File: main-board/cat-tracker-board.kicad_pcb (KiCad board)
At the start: 2 copper layers, 69.5 x 29 mm, 26 parts, among them J1 Conn_01x10, J2 USB_C_Receptacle_USB2.0, J3 Conn_01x03, J4 Conn_01x02, Q5 SI3443DDV-T1-GE3, SW1 PCM12SMTR, U1 ATSAMD21E18A-A, U2 LM3480-3.3, U4 RFM95W-915S2

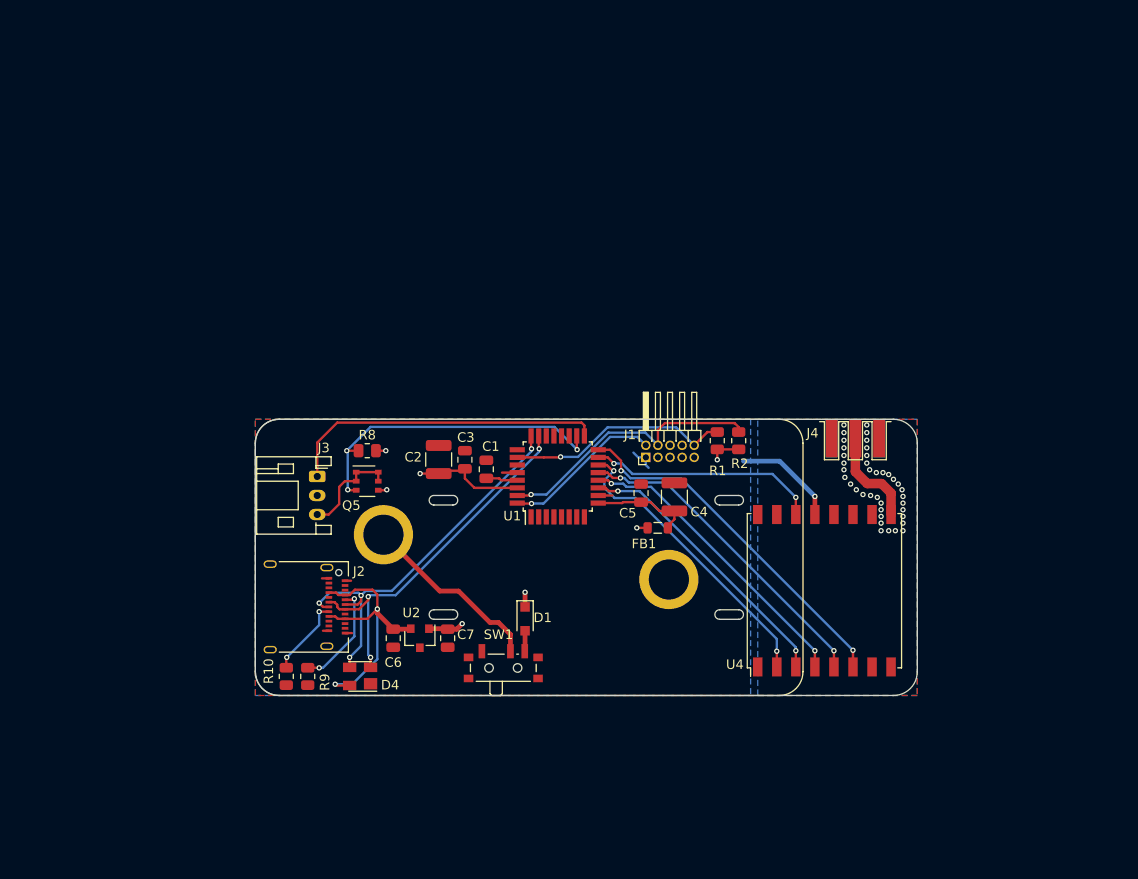
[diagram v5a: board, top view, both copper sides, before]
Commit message: Add L80 GPS, charge ic, and battery protection ic.
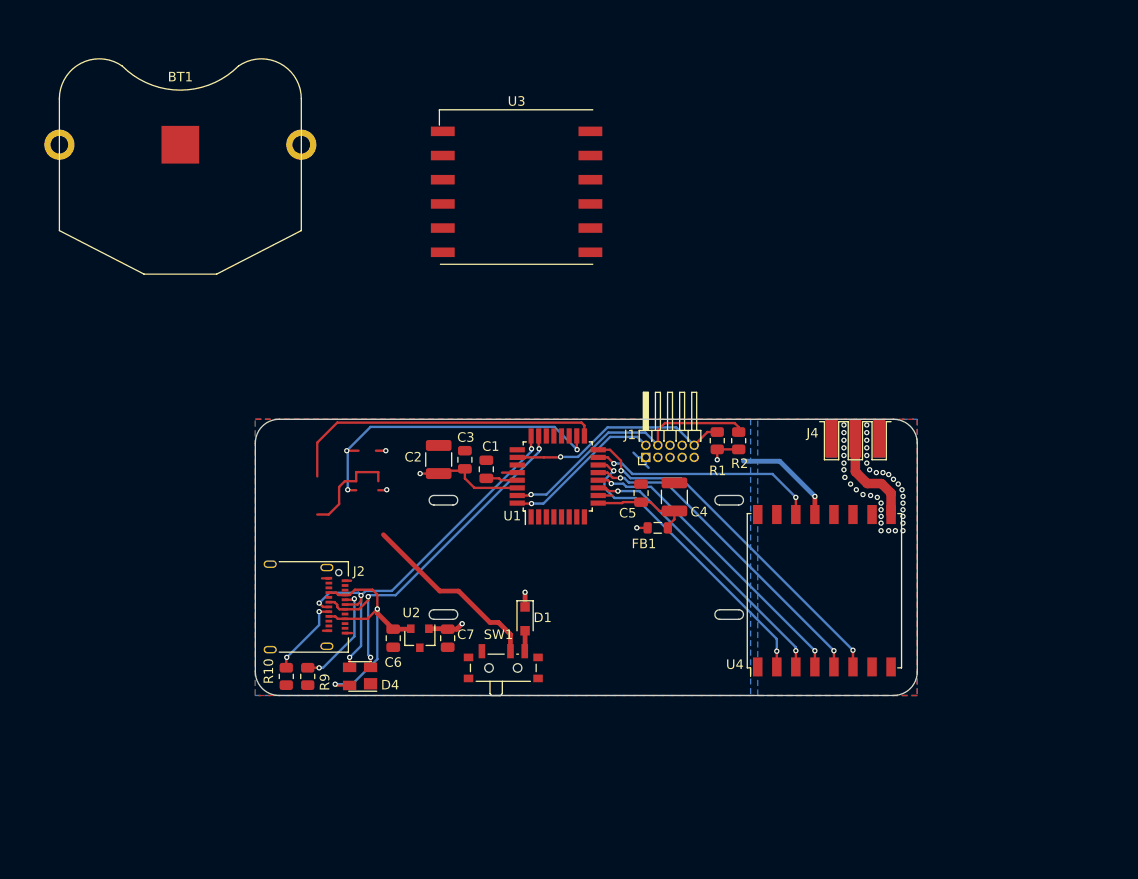
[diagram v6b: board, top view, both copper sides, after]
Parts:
- removed J3: Conn_01x03, Connector_JST:JST_PH_S3B-PH-K_1x03_P2.00mm_Horizontal
- removed Q5: SI3443DDV-T1-GE3, Package_SO:TSOP-6_1.65x3.05mm_P0.95mm
- removed R8: 100k, Resistor_SMD:R_0805_2012Metric
- added U3: L80-R, RF_GPS:Quectel_L80-R, F.Cu at (27.4, -24.4)
- BT1: value Battery -> Lir2477; footprint cat-tracker-board:battery-board -> colinholzman:Keystone_3039
- moved BT1 56.7 mm to (-7.87, -28.8)
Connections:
- U1 pad 17: /GPS_TX -> (no net)
- U1 pad 18: /GPS_EN -> (no net)
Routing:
- net (no net): track 0.00 -> 67.6 mm, vias 0 -> 3
- net /GPS_EN: track 33.9 -> 0.00 mm, vias 3 -> 0
- net /GPS_TX: track 33.7 -> 0.00 mm

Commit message: Annotate, assign footprints, and assign part numbers.
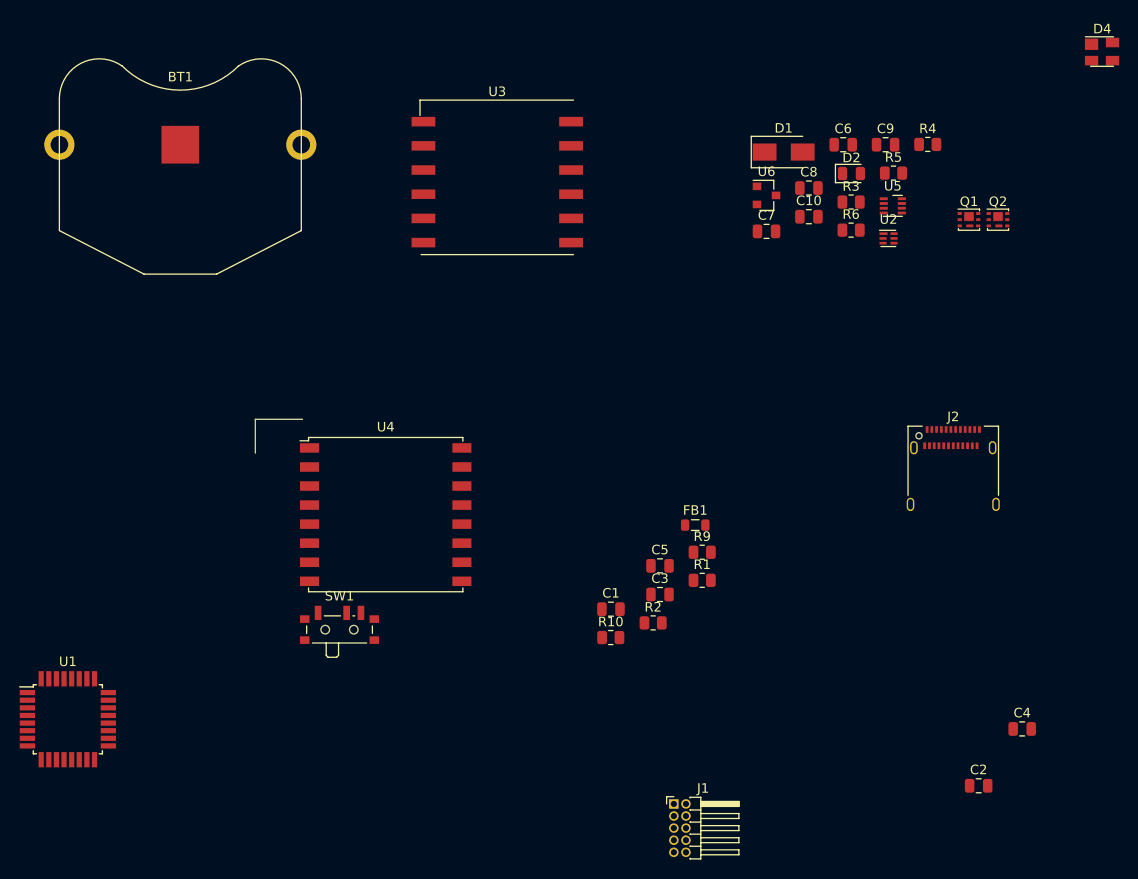
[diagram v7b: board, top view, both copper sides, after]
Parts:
- removed J4: Conn_01x02, cat-tracker-board:RF-Solutions-CON-SMA-EDGE-S
- added C10: 1 uF, Capacitor_SMD:C_0805_2012Metric, F.Cu at (58.1, -21.3)
- added C8: 0.1 uF, Capacitor_SMD:C_0805_2012Metric, F.Cu at (58.1, -24.3)
- added C9: 1 uF, Capacitor_SMD:C_0805_2012Metric, F.Cu at (66.2, -28.8)
- added D2: LED, LED_SMD:LED_0805_2012Metric, F.Cu at (62.6, -25.8)
- added Q1: CSD16301Q2, Package_SON:Texas_DQK, F.Cu at (74.9, -21.0)
- added Q2: CSD16301Q2, Package_SON:Texas_DQK, F.Cu at (78.0, -21.0)
- added R3: 2.2K, Resistor_SMD:R_0805_2012Metric, F.Cu at (62.6, -22.8)
- added R4: 330, Resistor_SMD:R_0805_2012Metric, F.Cu at (70.6, -28.9)
- added R5: 750, Resistor_SMD:R_0805_2012Metric, F.Cu at (67.0, -25.8)
- added R6: 14K, Resistor_SMD:R_0805_2012Metric, F.Cu at (62.6, -19.9)
- added U5: MCP73831-2ACI/MC, Package_DFN_QFN:DFN-8_2x2mm_P0.5mm, F.Cu at (66.9, -22.4)
- added U6: MCP1700T-3602E/TT, Package_TO_SOT_SMD:SOT-23, F.Cu at (53.7, -23.5)
- C2, C4: footprint Capacitor_SMD:C_1210_3225Metric -> Capacitor_SMD:C_0805_2012Metric
- C6, C7: value 0.1 uF -> 4.7 uF
- D1: value CUS08F30 -> SMAJ5.0A; footprint Diode_SMD:D_SOD-323_HandSoldering -> Diode_SMD:D_SMA
- J2: value USB_C_Receptacle_USB2.0 -> USB C
- U2: value LM3480-3.3 -> BQ29737DSER; footprint Package_TO_SOT_SMD:SOT-23 -> Package_SON:WSON-6_1.5x1.5mm_P0.5mm
- moved D4 101.8 mm to (88.9, -38.6), turned to 0 degrees
- moved J2 70.2 mm to (73.3, 6.10), turned to 0 degrees
- moved C6 70.1 mm to (61.7, -28.8), turned to 0 degrees
- moved C2 66.2 mm to (75.9, 38.5), turned to 0 degrees
- moved U2 64.7 mm to (66.5, -19.0), turned to 0 degrees
- moved U1 57.4 mm to (-19.7, 31.5), turned to 0 degrees
- moved D1 56.0 mm to (55.5, -28.1), turned to 0 degrees
- moved C7 54.3 mm to (53.7, -19.7), turned to 0 degrees
- moved U4 46.8 mm to (13.7, 10.0), turned to 0 degrees
- moved C4 43.9 mm to (80.5, 32.5), turned to 0 degrees
- moved R9 43.4 mm to (46.9, 14.0), turned to 0 degrees
- moved J1 36.5 mm to (43.9, 40.4), turned to 0 degrees
- moved G*** 36.4 mm to (94.0, -4.19)
- moved R10 34.3 mm to (37.3, 22.9), turned to 0 degrees
- moved C3 24.9 mm to (42.5, 18.4), turned to 0 degrees
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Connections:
- BT1 pad 2: /GND -> Net-(BT1-Pad2)
- C2 pad 1: /+3V3 -> /VDD
- C3 pad 2: /+3V3 -> /VDD
- C6 pad 1: /GND -> /VUSB
- C6 pad 2: /VUSB -> /GND
- C7 pad 1: /GND -> /VBAT
- C7 pad 2: /+3V3 -> /GND
- D1 pad 1: /+3V3 -> /VUSB
- D1 pad 2: Net-(D1-Pad2) -> /GND
- FB1 pad 1: /+3V3 -> /VDD
- J1 pad 1: /+3V3 -> (no net)
- R1 pad 1: /+3V3 -> /VDD
- R2 pad 1: /+3V3 -> /VDD
- SW1 pad 3: Net-(D1-Pad2) -> Net-(C9-Pad1)
- U1 pad 30: /+3V3 -> /VDD
- U2 pad 1: /+3V3 -> (no net)
- U2 pad 2: /VUSB -> Net-(Q1-Pad3)
- U2 pad 3: /GND -> Net-(Q2-Pad3)
- U4 pad 13: /+3V3 -> /VDD
- U4 pad 9: Net-(J4-Pad1) -> (no net)
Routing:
- net (no net): track 67.6 -> 0.00 mm, vias 3 -> 0
- net /USBDP: track 42.4 -> 0.00 mm, vias 4 -> 0
- net /USBDM: track 38.8 -> 0.00 mm, vias 3 -> 0
- net /RFM_RESET: track 37.8 -> 0.00 mm, vias 2 -> 0
- net /+3V3: track 37.2 -> 0.00 mm, vias 8 -> 0
- net /NSS: track 34.2 -> 0.00 mm, vias 2 -> 0
- net /SCK: track 31.9 -> 0.00 mm, vias 2 -> 0
- net /MISO: track 31.7 -> 0.00 mm, vias 2 -> 0
- net /VUSB: track 29.8 -> 0.00 mm, vias 2 -> 0
- net /MOSI: track 29.7 -> 0.00 mm, vias 2 -> 0
- net /SWCLK: track 29.1 -> 0.00 mm, vias 1 -> 0
- net /RFM_INT: track 24.3 -> 0.00 mm, vias 2 -> 0
- net /nRESET: track 23.7 -> 0.00 mm, vias 1 -> 0
- net /VBAT: track 19.4 -> 0.00 mm
- net /SWDIO: track 16.8 -> 0.00 mm, vias 1 -> 0
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- removed copper zone on B.Cu, net /+3V3
- removed copper zone on B.Cu, net /GND
- removed copper zone on F.Cu, net /GND
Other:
- board size 69.5 x 29 mm -> 5 x 3.6 mm
- board text removed: "OFF"
- board text removed: "ON"

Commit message: Change usb to micro B type.
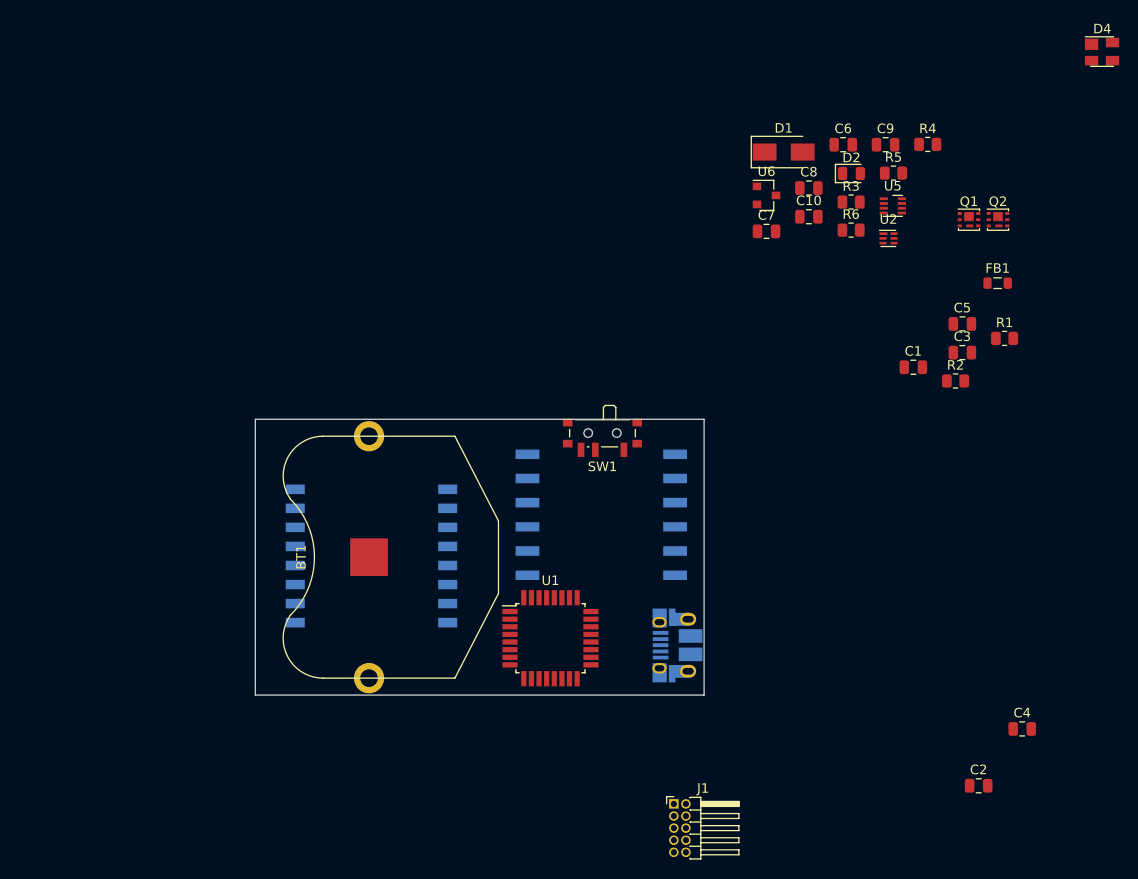
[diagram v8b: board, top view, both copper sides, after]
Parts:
- removed J2: USB C, Connector_USB:USB_C_Receptacle_Amphenol_12401610E4-2A
- removed R10, R9: 5.1k, Resistor_SMD:R_0805_2012Metric
- added J3: USB_B_Micro, Connector_USB:USB_Micro-B_Amphenol_10103594-0001LF_Horizontal, B.Cu at (44.3, 23.7)
- U3, U4: moved to B.Cu
- moved U1 51.4 mm to (31.0, 23.0)
- moved BT1 47.6 mm to (11.9, 14.5), turned to 90 degrees
- moved C3 40.7 mm to (74.2, -7.00)
- moved C5 40.7 mm to (74.2, -10.0)
- moved FB1 40.7 mm to (77.9, -14.3)
- moved R1 40.7 mm to (78.7, -8.49)
- moved R2 40.7 mm to (73.5, -4.02)
- moved C1 40.7 mm to (69.1, -5.46)
- moved U3 36.6 mm to (36.3, 9.53), turned to 180 degrees
- moved SW1 34.1 mm to (36.4, 1.78), turned to 180 degrees
- moved U4 4.59 mm to (12.2, 14.4), turned to 180 degrees
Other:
- board size 5 x 3.6 mm -> 47.1 x 29 mm
